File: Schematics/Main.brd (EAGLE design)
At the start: 69.8 x 32.7 mm, 27 parts, among them IC1 ICL7611ACPA, Q2 2N5486, Q3 2N5486, U1 ENCODER_2LED, X1 USBPTH

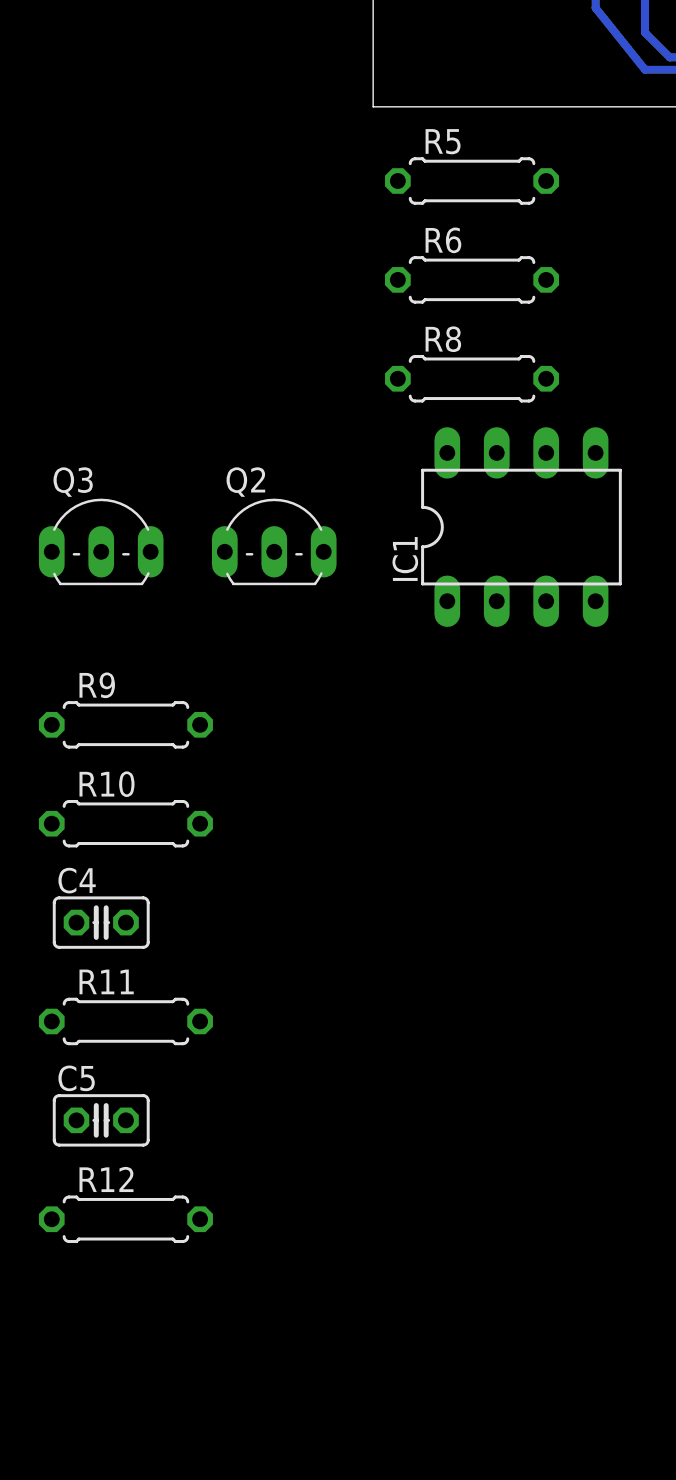
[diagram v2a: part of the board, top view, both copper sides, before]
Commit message: Using VGA and VCR
Using variable gain amplifier for input and a VCR to inject signals

Signed-off-by: Aljaž "g5pw" Srebrnič <a2piratesoft@gmail.com>
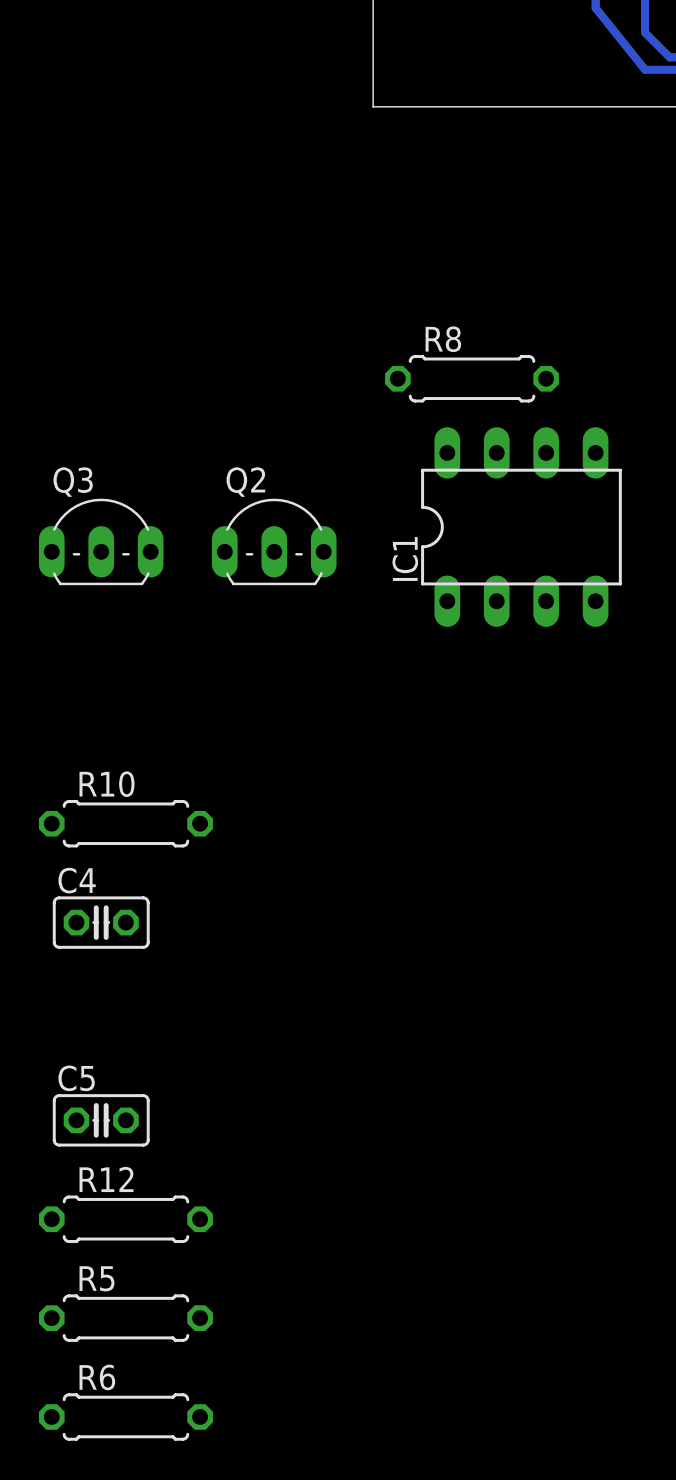
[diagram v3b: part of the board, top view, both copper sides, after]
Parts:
- removed R11, R9: (no value), rcl:0207/7
- moved R5 61.1 mm to (-12.7, -63.5)
- moved R6 61.1 mm to (-12.7, -68.6)
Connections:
- new net N$21: Q3.2, R6.1
- net GND: now also R5.1; no longer IC1.3, Q2.2
- net N$13: now also Q2.2, R5.2; no longer R6.2, R8.1
- net N$14: now also IC1.3, R6.2; no longer Q3.2, R5.1
- net N$17: no longer R9.1
- net N$18: no longer R11.1
- net N$8: now also R8.1; no longer R5.2, R6.1
- net VDD: no longer R11.2, R9.2
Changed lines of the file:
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@@
 <element name="R4" library="rcl" package="0207/7" value="10k" x="40.64" y="21.59" rot="R90"/>
 <element name="R7" library="rcl" package="0207/7" value="81" x="16.51" y="22.86"/>
-<element name="R5" library="rcl" package="0207/7" value="" x="5.08" y="-5.08"/>
-<element name="R6" library="rcl" package="0207/7" value="" x="5.08" y="-10.16"/>
 <element name="R8" library="rcl" package="0207/7" value="" x="5.08" y="-15.24"/>
 <element name="IC1" library="maxim" package="DIL08" value="ICL7611ACPA" x="7.62" y="-22.86">
@@
 <element name="Q2" library="transistor-fet" package="TO92-" value="2N5486" x="-5.08" y="-24.13"/>
 <element name="Q3" library="transistor-fet" package="TO92-" value="2N5486" x="-13.97" y="-24.13"/>
-<element name="R9" library="rcl" package="0207/7" value="" x="-12.7" y="-33.02"/>
 <element name="R10" library="rcl" package="0207/7" value="" x="-12.7" y="-38.1"/>
 <element name="C4" library="rcl" package="C025-025X050" value="" x="-13.97" y="-43.18"/>
-<element name="R11" library="rcl" package="0207/7" value="" x="-12.7" y="-48.26"/>
 <element name="C5" library="rcl" package="C025-025X050" value="" x="-13.97" y="-53.34"/>
 <element name="R12" library="rcl" package="0207/7" value="" x="-12.7" y="-58.42"/>
+<element name="R5" library="rcl" package="0207/7" value="" x="-12.7" y="-63.5"/>
+<element name="R6" library="rcl" package="0207/7" value="" x="-12.7" y="-68.58"/>
 </elements>
 <signals>
@@
 <contactref element="SV1" pad="2"/>
 <wire x1="7.62" y1="26.67" x2="7.62" y2="29.21" width="0.4064" layer="16"/>
-<contactref element="IC1" pad="3"/>
-<contactref element="Q2" pad="2"/>
 <contactref element="C4" pad="2"/>
 <contactref element="C5" pad="2"/>
+<contactref element="R5" pad="1"/>
+<wire x1="-12.7" y1="-53.34" x2="-16.51" y2="-63.5" width="0" layer="19" extent="1-1"/>
 <wire x1="-12.7" y1="-43.18" x2="-12.7" y2="-53.34" width="0" layer="19" extent="1-1"/>
-<wire x1="-5.08" y1="-24.13" x2="-12.7" y2="-43.18" width="0" layer="19" extent="1-1"/>
-<wire x1="8.89" y1="-26.67" x2="-5.08" y2="-24.13" width="0" layer="19" extent="1-1"/>
-<wire x1="3.175" y1="13.335" x2="-5.08" y2="-24.13" width="0" layer="19" extent="16-16"/>
+<wire x1="3.175" y1="13.335" x2="-12.7" y2="-43.18" width="0" layer="19" extent="16-16"/>
 </signal>
 <signal name="N$2">
@@
 <wire x1="8.89" y1="22.86" x2="12.7" y2="22.86" width="0.4064" layer="16"/>
 <contactref element="Q3" pad="3"/>
-<contactref element="R9" pad="2"/>
-<contactref element="R11" pad="2"/>
 <wire x1="12.7" y1="22.86" x2="38.1" y2="24.13" width="0" layer="19" extent="16-16"/>
 <wire x1="-16.51" y1="-24.13" x2="8.89" y2="22.86" width="0" layer="19" extent="16-16"/>
-<wire x1="-8.89" y1="-33.02" x2="-16.51" y2="-24.13" width="0" layer="19" extent="1-1"/>
-<wire x1="-8.89" y1="-48.26" x2="-8.89" y2="-33.02" width="0" layer="19" extent="1-1"/>
 </signal>
 <signal name="SDIN">
@@
 <contactref element="IC1" pad="4"/>
 </signal>
-<signal name="N$8">
-<contactref element="R5" pad="2"/>
-<contactref element="R6" pad="1"/>
-<contactref element="Q2" pad="3"/>
-<wire x1="1.27" y1="-10.16" x2="-7.62" y2="-24.13" width="0" layer="19" extent="1-1"/>
-<wire x1="8.89" y1="-5.08" x2="1.27" y2="-10.16" width="0" layer="19" extent="1-1"/>
-</signal>
-<signal name="N$13">
+<signal name="N$14">
+<contactref element="LSP1" pad="MP"/>
+<contactref element="IC1" pad="3"/>
 <contactref element="R6" pad="2"/>
-<contactref element="IC1" pad="2"/>
-<contactref element="R8" pad="1"/>
-<wire x1="1.27" y1="-15.24" x2="6.35" y2="-26.67" width="0" layer="19" extent="1-1"/>
-<wire x1="8.89" y1="-10.16" x2="1.27" y2="-15.24" width="0" layer="19" extent="1-1"/>
-</signal>
-<signal name="N$14">
-<contactref element="R5" pad="1"/>
-<contactref element="LSP1" pad="MP"/>
-<contactref element="Q3" pad="2"/>
-<wire x1="1.27" y1="-5.08" x2="-13.97" y2="-24.13" width="0" layer="19" extent="1-1"/>
-<wire x1="2.54" y1="10.16" x2="1.27" y2="-5.08" width="0" layer="19" extent="1-1"/>
+<wire x1="8.89" y1="-26.67" x2="-8.89" y2="-68.58" width="0" layer="19" extent="1-1"/>
+<wire x1="2.54" y1="10.16" x2="8.89" y2="-26.67" width="0" layer="19" extent="1-1"/>
 </signal>
 <signal name="N$16">
@@
 <signal name="N$17">
 <contactref element="U$1" pad="14"/>
-<contactref element="R9" pad="1"/>
 <contactref element="R10" pad="1"/>
-<wire x1="-16.51" y1="-33.02" x2="-16.51" y2="-38.1" width="0" layer="19" extent="1-1"/>
-<wire x1="19.05" y1="8.89" x2="-16.51" y2="-33.02" width="0" layer="19" extent="1-1"/>
+<wire x1="19.05" y1="8.89" x2="-16.51" y2="-38.1" width="0" layer="19" extent="1-1"/>
 </signal>
 <signal name="N$18">
 <contactref element="U$1" pad="7"/>
-<contactref element="R11" pad="1"/>
 <contactref element="R12" pad="1"/>
-<wire x1="-16.51" y1="-48.26" x2="-16.51" y2="-58.42" width="0" layer="19" extent="1-1"/>
-<wire x1="19.05" y1="16.51" x2="-16.51" y2="-48.26" width="0" layer="19" extent="1-1"/>
+<wire x1="19.05" y1="16.51" x2="-16.51" y2="-58.42" width="0" layer="19" extent="1-1"/>
 </signal>
 <signal name="N$19">
@@
 <wire x1="-11.43" y1="-24.13" x2="-15.24" y2="-53.34" width="0" layer="19" extent="1-1"/>
 </signal>
+<signal name="N$8">
+<contactref element="R8" pad="1"/>
+<contactref element="Q2" pad="3"/>
+<wire x1="1.27" y1="-15.24" x2="-7.62" y2="-24.13" width="0" layer="19" extent="1-1"/>
+</signal>
+<signal name="N$13">
+<contactref element="IC1" pad="2"/>
+<contactref element="R5" pad="2"/>
+<contactref element="Q2" pad="2"/>
+<wire x1="-5.08" y1="-24.13" x2="-8.89" y2="-63.5" width="0" layer="19" extent="1-1"/>
+<wire x1="6.35" y1="-26.67" x2="-5.08" y2="-24.13" width="0" layer="19" extent="1-1"/>
+</signal>
+<signal name="N$21">
+<contactref element="Q3" pad="2"/>
+<contactref element="R6" pad="1"/>
+<wire x1="-13.97" y1="-24.13" x2="-16.51" y2="-68.58" width="0" layer="19" extent="1-1"/>
+</signal>
 </signals>
